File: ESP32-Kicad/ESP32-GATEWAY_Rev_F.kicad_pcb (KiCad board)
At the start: 2 copper layers, 50.8 x 62.2 mm, 97 parts, among them CON1 NA(NH1x20), Q3 Q12MHz/20pF/30ppm/2P/HC-49SM(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, Q4 BC817-40(SOT23), Q5 BC817-40(SOT23), T1 DTC114YKA, U2 SY8089AAAC(SOT23-5), U3 ESP32-WROOM-32D-4MB, U4 LAN8710A-EZC(QFN32), U5 CH340T(SSOP20W)

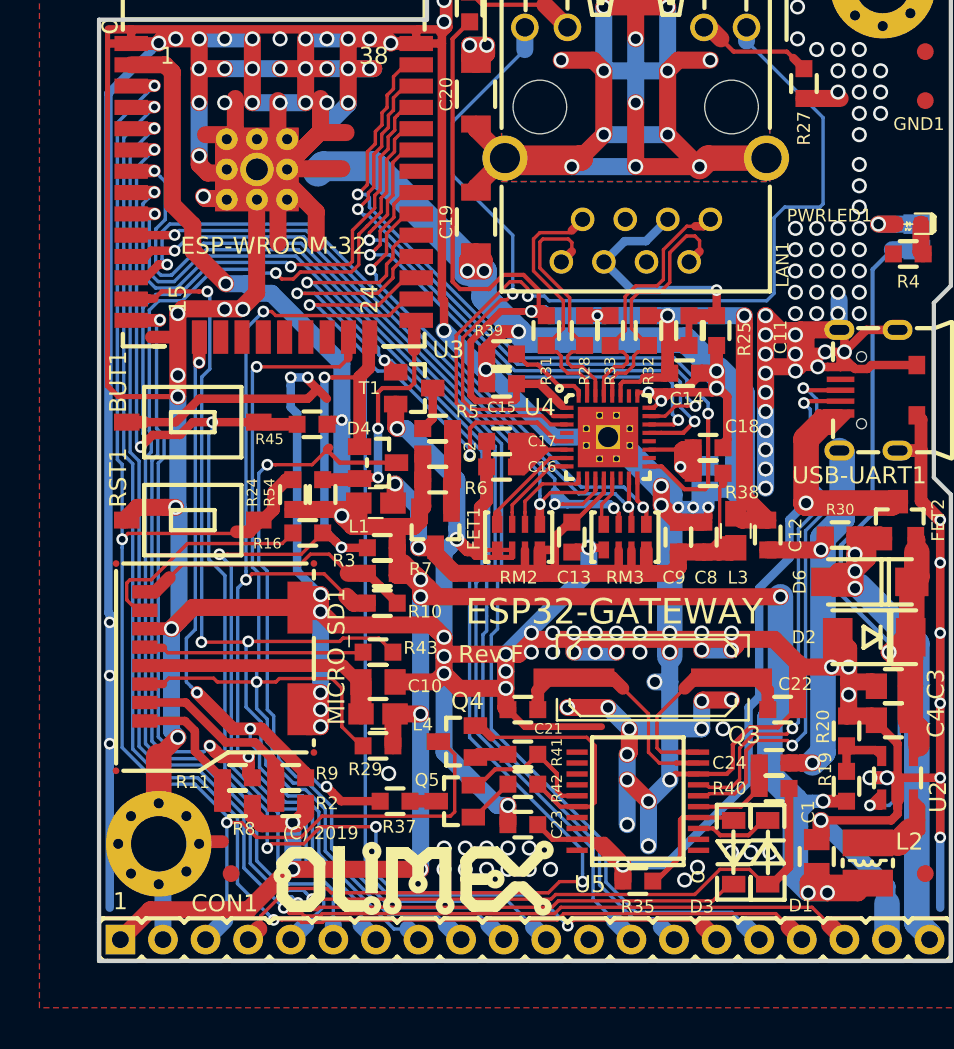
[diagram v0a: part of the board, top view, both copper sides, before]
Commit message: Proyecto de kicad actualizado.
 Se eliminó completamente la sección de la MicroSD
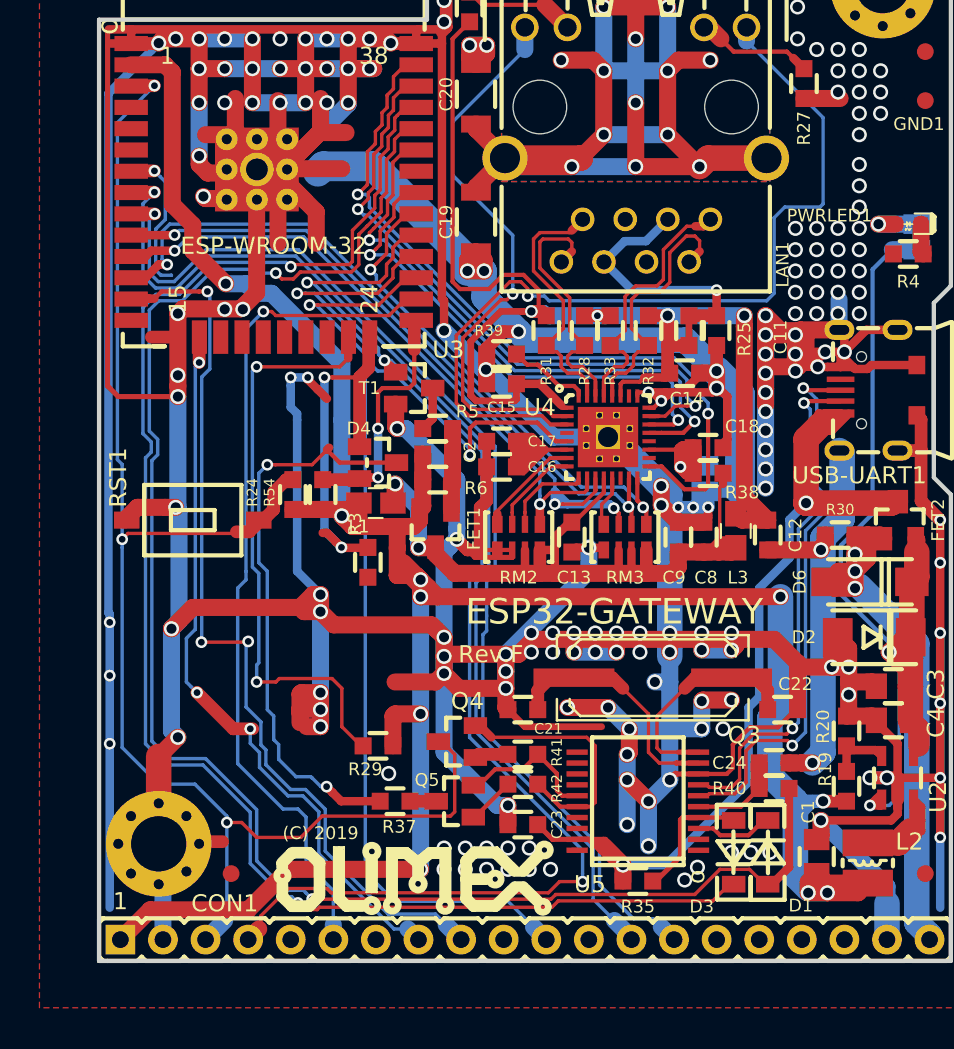
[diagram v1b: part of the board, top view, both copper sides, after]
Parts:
- removed BUT1: T1107A(6x3,8x2,5MM), OLIMEX_Buttons-FP:T1107A(6x3,8x2,5MM)
- removed C10: 47uF/6.3V/20%/X5R/C0805, OLIMEX_RLC-FP:C_0805_5MIL_DWS
- removed L4: FB0805/600R/2A, OLIMEX_RLC-FP:L_0805_5MIL_DWS
- removed MICRO_SD1: TFC-WXCP11-08-LF, OLIMEX_Connectors-FP:TFC-WXCP11-08-LF
- removed R10, R11, R9: NA/R0603, OLIMEX_RLC-FP:R_0603_5MIL_DWS
- removed R16: 220R/R0603, OLIMEX_RLC-FP:R_0603_5MIL_DWS
- removed R2, R7, R8: 2.2k/R0603, OLIMEX_RLC-FP:R_0603_5MIL_DWS
- removed R43: 10R/R0603, OLIMEX_RLC-FP:R_0603_5MIL_DWS
- removed R45: 10k/R0603, OLIMEX_RLC-FP:R_0603_5MIL_DWS
- moved R3 1.22 mm to (85.6, 105.5), turned to 90 degrees
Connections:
- CON1 pad 10: /GPIO15\HS2_CMD -> Net-(CON1-Pad10)
- CON1 pad 15: /GPI34\BUT1 -> Net-(CON1-Pad15)
- CON1 pad 16: /GPI35 -> Net-(CON1-Pad16)
- CON1 pad 17: /GPI36 -> Net-(CON1-Pad17)
- CON1 pad 18: /GPI39 -> Net-(CON1-Pad18)
- CON1 pad 5: /GPIO2\HS2_DATA0 -> Net-(CON1-Pad5)
- CON1 pad 7: /GPIO12\HS2_DATA2 -> Net-(CON1-Pad7)
- R3 pad 1: +3V3 -> GND
- U3 pad 6: /GPI34\BUT1 -> /GPI34
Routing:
- net /GPI34\BUT1: track 88.6 -> 0.00 mm, vias 6 -> 0
- net /GPI39: track 88.3 -> 0.12 mm, vias 2 -> 0
- net /GPI36: track 88.1 -> 0.12 mm, vias 2 -> 0
- net /GPI35: track 74.2 -> 9.01 mm
- net /GPIO12\HS2_DATA2: track 49.1 -> 0.00 mm, vias 3 -> 0
- net /GPIO2\HS2_DATA0: track 56.0 -> 21.9 mm, vias 3 -> 2
- net /GPIO15\HS2_CMD: track 66.7 -> 34.9 mm
- net Net-(MICRO_SD1-Pad8): track 17.2 -> 0.00 mm
- net Net-(C10-Pad1): track 15.3 -> 0.00 mm
- net GND: track 790.1 -> 776.2 mm
- net Net-(MICRO_SD1-Pad7): track 13.5 -> 0.00 mm
- net Net-(MICRO_SD1-Pad5): track 13.2 -> 0.00 mm
- net Net-(MICRO_SD1-Pad2): track 12.6 -> 0.00 mm
- net /GPIO14\HS2_CLK: track 63.6 -> 54.6 mm
- net +3V3: track 168.5 -> 159.8 mm, vias 13 -> 10
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
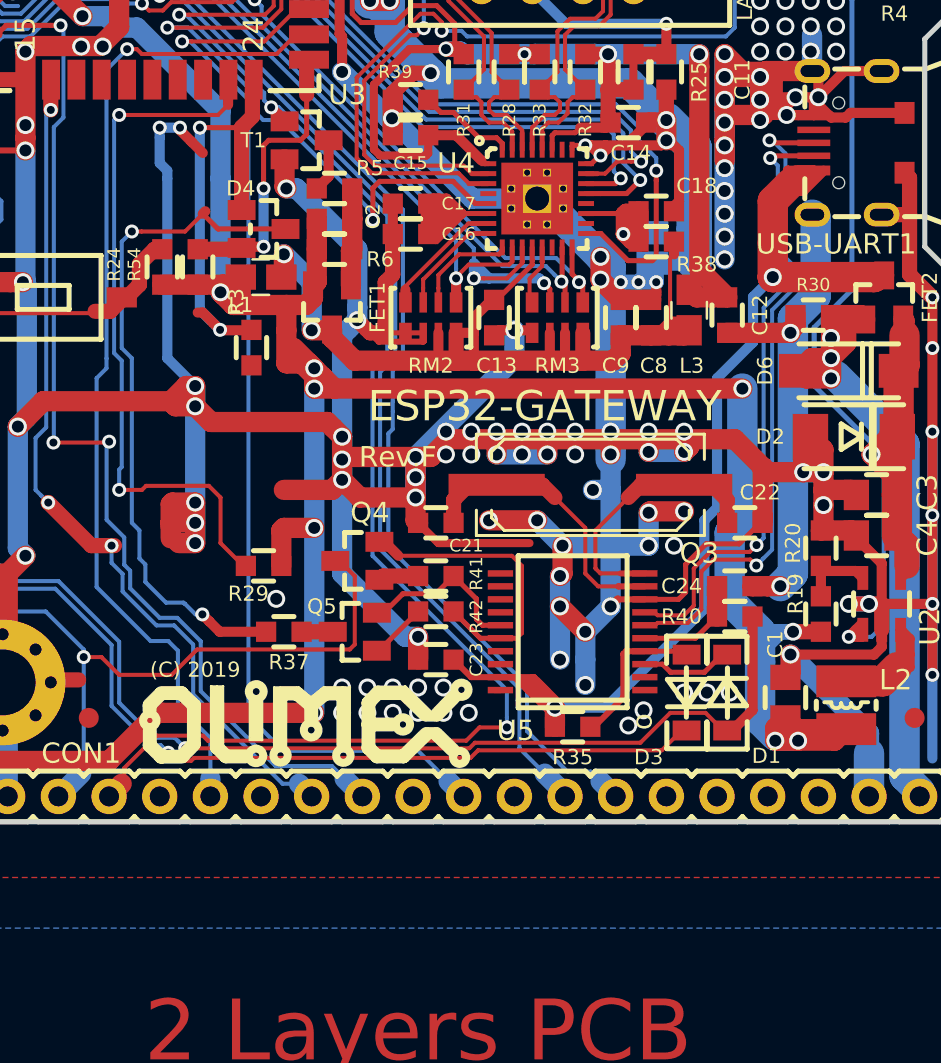
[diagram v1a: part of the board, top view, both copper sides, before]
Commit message: Proyecto de kicad actualizado
Se retiró la parte del programador USB y otras menores asociadas a esta.
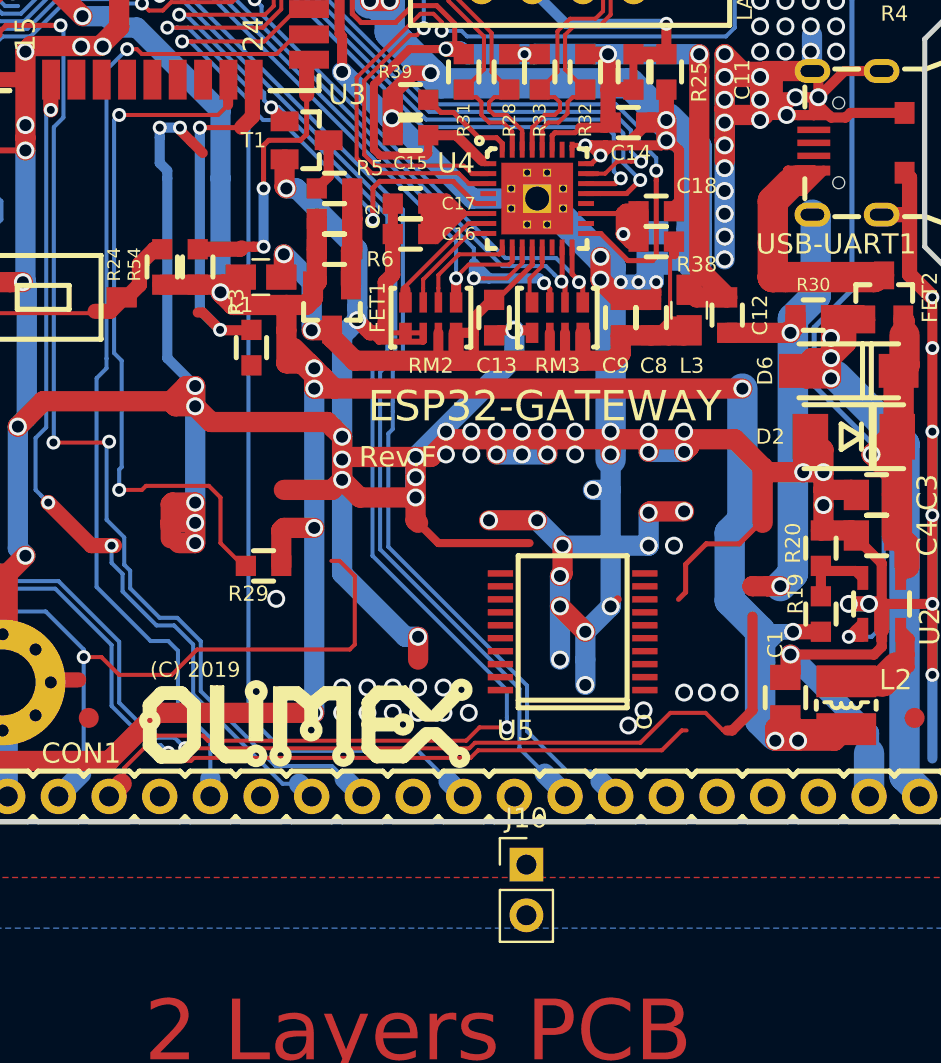
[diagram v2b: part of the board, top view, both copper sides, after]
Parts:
- removed C21, C22: 27pF/50V/5%/C0G/C0603, OLIMEX_RLC-FP:C_0603_5MIL_DWS
- removed C23: 22uF/6.3V/20%/X5R/C0603, OLIMEX_RLC-FP:C_0603_5MIL_DWS
- removed C24: 100nF/50V/20%/Y5V/C0603, OLIMEX_RLC-FP:C_0603_5MIL_DWS
- removed D1, D3: 1N5819S4/SOD123, OLIMEX_Diodes-FP:SOD-123_1C-2A_KA
- removed D4: BAT54C(SOT23-3), OLIMEX_Diodes-FP:SOT23-3
- removed Q3: Q12MHz/20pF/30ppm/2P/HC-49SM(SMD), OLIMEX_Crystal-FP:Q_49U3HMS
- removed Q4, Q5: BC817-40(SOT23), OLIMEX_Transistors-FP:SOT23
- removed R35, R40: 10k/R0603, OLIMEX_RLC-FP:R_0603_5MIL_DWS
- removed R37: 220R/R0603, OLIMEX_RLC-FP:R_0603_5MIL_DWS
- removed R41, R42: 1k/R0603, OLIMEX_RLC-FP:R_0603_5MIL_DWS
- added J10: Conn_01x02_Male, Connector_PinHeader_2.54mm:PinHeader_1x02_P2.54mm_Vertical, F.Cu at (99.4, 131.4)
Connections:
- U5 pad 8: GND -> Net-(U5-Pad8)
- USB-UART1 pad 2: Net-(U5-Pad7) -> Net-(USB-UART1-Pad2)
- USB-UART1 pad 3: Net-(U5-Pad6) -> Net-(USB-UART1-Pad3)
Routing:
- net /+5V_USB: track 58.6 -> 19.1 mm, vias 2 -> 0
- net /D_Com: track 33.9 -> 0.00 mm, vias 2 -> 0
- net Net-(U5-Pad6): track 33.4 -> 0.00 mm, vias 2 -> 0
- net Net-(U5-Pad7): track 30.8 -> 0.00 mm, vias 2 -> 0
- net Net-(U5-Pad16): track 15.1 -> 0.00 mm
- net Net-(U5-Pad9): track 14.4 -> 0.00 mm
- net Net-(U5-Pad10): track 14.3 -> 0.00 mm
- net Net-(U5-Pad15): track 8.58 -> 0.00 mm
- net Net-(U5-Pad4): track 7.75 -> 0.00 mm
- net Net-(U5-Pad5): track 5.59 -> 0.00 mm
- net Net-(U5-Pad3): track 4.66 -> 0.00 mm
- net /GPIO2\HS2_DATA0: track 21.9 -> 17.8 mm
- net GND: track 776.2 -> 773.2 mm
- net Net-(Q5-Pad1): track 2.88 -> 0.00 mm
- net Net-(Q4-Pad1): track 2.02 -> 0.00 mm
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
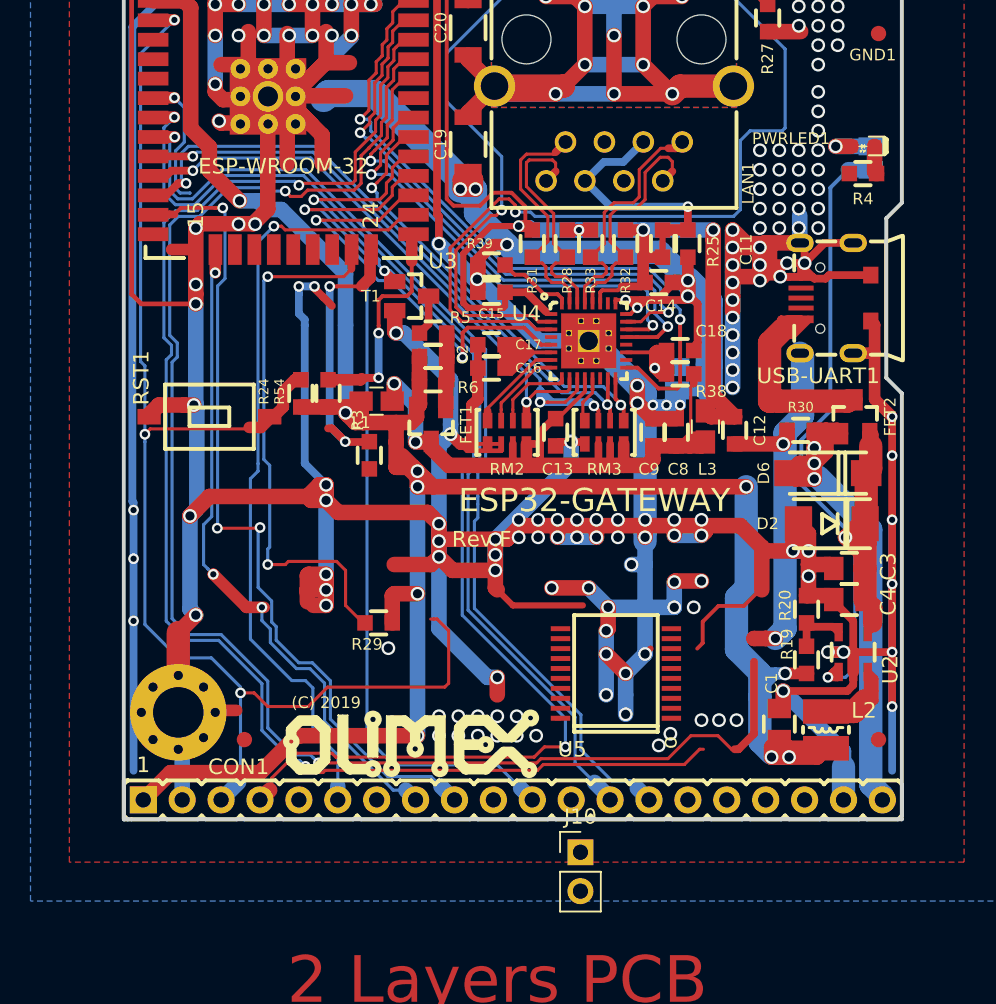
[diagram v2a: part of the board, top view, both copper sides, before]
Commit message: Proyecto de Kicad actualizado
Fuente corregida. Programador agregado. Cambios menores.
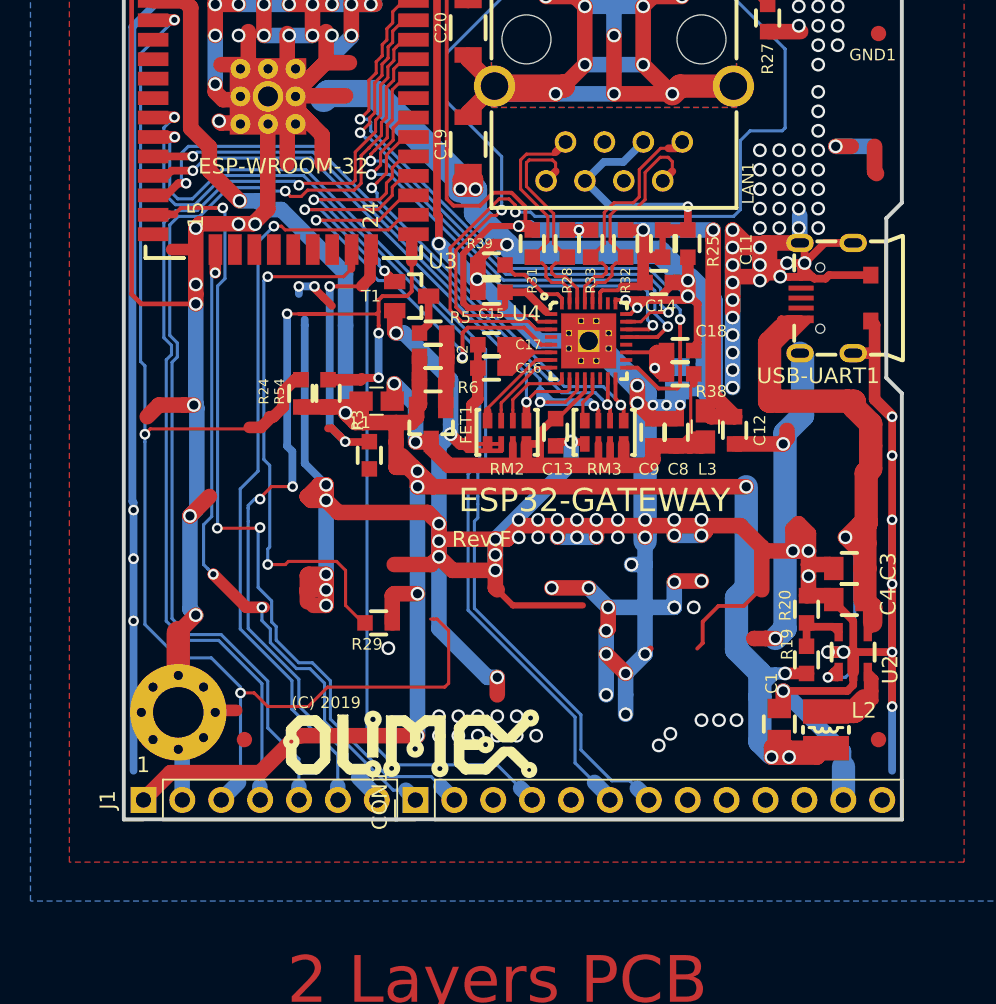
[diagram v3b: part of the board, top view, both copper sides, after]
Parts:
- removed D2: SMBJ6.0A(DO-214AA), OLIMEX_Diodes-FP:DO214AA_1(K)-2(A)
- removed D6: 1N5822/SS34/SMA, OLIMEX_Diodes-FP:SMA-KA
- removed FET2: WPM2015-3/TR, OLIMEX_Transistors-FP:SOT23
- removed J10: Conn_01x02_Male, Connector_PinHeader_2.54mm:PinHeader_1x02_P2.54mm_Vertical
- removed LED_E1: Closed, OLIMEX_Jumpers-FP:SJ
- removed PWRLED1: LED/RED/0603, OLIMEX_LEDs-FP:LED_0603_KA
- removed R30: 1M/R0603, OLIMEX_RLC-FP:R_0603_5MIL_DWS
- removed R4: 2.2k/R0603, OLIMEX_RLC-FP:R_0603_5MIL_DWS
- removed RST1: T1107A(6x3,8x2,5MM), OLIMEX_Buttons-FP:T1107A(6x3,8x2,5MM)
- removed U5: CH340T(SSOP20W), OLIMEX_IC-FP:SSOP-20W
- added J1: Conn_01x07_Male, Connector_PinHeader_2.54mm:PinHeader_1x07_P2.54mm_Vertical, F.Cu at (70.9, 128.0)
- C1: value 47uF/6.3V/20%/X5R/C0805 -> 10uF/6.3V/20%/X5R/C0805/1mΩ
- C3, C4: value 47uF/6.3V/20%/X5R/C0805 -> 4.7uF/6.3V/20%/X5R/C0805/1mΩ
- CON1: value NA(NH1x20) -> Conn_01x13_Male; footprint OLIMEX_Connectors-FP:HN1x20 -> Connector_PinHeader_2.54mm:PinHeader_1x13_P2.54mm_Vertical
- L2: value 2.2uH/1.5A/DCR=72mR/20%/3.00x3.00x1.50mm/CD32(NR3015T2R2M) -> 2.2uH/1.5A/DCR=35mR/20%/3.00x3.00x1.50mm/CD32(NR3015T2R2M)
- R19: value 220k/R0603 -> 442k/1%/50mW/R0603
- R20: value 49.9k/1%/R0603 -> 100k/1%/63mw/R0603
- R54: value NA/R0603 -> 10K/R0603
- U2: value SY8089AAAC(SOT23-5) -> TLV62569DBVT(SOT23-5)
- moved CON1 6.36 mm to (88.6, 128.0), turned to 90 degrees
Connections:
- CON1 pad 1: +3V3 -> /GPIO13\HS2_DATA3
- CON1 pad 11: /GPIO16 -> Net-(CON1-Pad11)
- CON1 pad 12: Net-(CON1-Pad12) -> GND
- CON1 pad 13: /GPIO32 -> Net-(CON1-Pad13)
- CON1 pad 2: GND -> /GPIO14\HS2_CLK
- CON1 pad 3: /ESP_EN -> Net-(CON1-Pad3)
- CON1 pad 4: /GPIO5\PHY_PWR -> /GPIO16
- CON1 pad 6: /GPIO4\HS2_DATA1 -> /GPIO32
- CON1 pad 7: Net-(CON1-Pad7) -> /GPIO33\LED
- CON1 pad 8: /GPIO13\HS2_DATA3 -> Net-(CON1-Pad8)
- CON1 pad 9: /GPIO14\HS2_CLK -> Net-(CON1-Pad9)
- USB-UART1 pad 1: /+5V_USB -> +5V
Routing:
- net /GPIO5\PHY_PWR: track 75.0 -> 16.2 mm, vias 3 -> 2
- net /GPIO0: track 14.6 -> 59.4 mm, vias 2 -> 5
- net +5V_EXT: track 39.9 -> 0.00 mm, vias 3 -> 0
- net /GPIO3\U0RXD: track 100.0 -> 66.8 mm, vias 2 -> 1
- net /GPIO1\U0TXD: track 93.2 -> 69.1 mm, vias 2 -> 1
- net /+5V_USB: track 19.1 -> 0.00 mm
- net +5V: track 64.9 -> 55.0 mm, vias 3 -> 2
- net /GPI35: track 9.01 -> 0.00 mm, vias 1 -> 0
- net Net-(PWRLED1-Pad1): track 1.83 -> 0.00 mm
- net GND: track 773.2 -> 771.6 mm, vias 197 -> 198

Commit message: Proyecto de kicad actualizado.
Se agregaron los conectores adecuados y se rutearon los gpio para estos. Queda pendiente ubicarlos correctamente para evitar el solapamiento de estos. Se acomodaron algunas resistencias y se eliminaron pistas viejas innecesarias.
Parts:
- removed CON1: Conn_01x13_Male, Connector_PinHeader_2.54mm:PinHeader_1x13_P2.54mm_Vertical
- removed USB-UART1: MISB-SWMM-5B-LF(USB_MICRO), OLIMEX_Connectors-FP:USB-MICRO_MISB-SWMM-5B_LF
- added PUERTA1: Conn_01x02_Female, Connector_Molex:Molex_KK-254_AE-6410-02A_1x02_P2.54mm_Vertical, F.Cu at (107.3, 124.6)
- added PUERTA2: Conn_01x02_Female, Connector_Molex:Molex_KK-254_AE-6410-02A_1x02_P2.54mm_Vertical, F.Cu at (103.6, 124.6)
- added TEMP1: Conn_01x03_Female, Connector_Molex:Molex_KK-254_AE-6410-03A_1x03_P2.54mm_Vertical, F.Cu at (95.4, 122.3)
- added TEMP2: Conn_01x03_Female, Connector_Molex:Molex_KK-254_AE-6410-03A_1x03_P2.54mm_Vertical, F.Cu at (91.6, 122.2)
- added USB-UART2: USB_B_Micro, Connector_USB:USB_Micro-B_Amphenol_10104110_Horizontal, F.Cu at (115.5, 95.3)
- J1: footprint Connector_PinHeader_2.54mm:PinHeader_1x07_P2.54mm_Vertical -> Connector_PinHeader_2.54mm:PinHeader_1x07_P2.54mm_Horizontal
- moved R29 19.8 mm to (79.0, 98.0)
- moved Logo-OlimexBIG 13.6 mm to (79.1, 114.5)
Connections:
- U3 pad 13: /GPIO14\HS2_CLK -> /GPIO14\TEMP2
- U3 pad 16: /GPIO13\HS2_DATA3 -> /GPIO13\TEMP1
- U3 pad 8: /GPIO32 -> /GPIO32\PUERTA1
- U3 pad 9: /GPIO33\LED -> /GPIO33\PUERTA2
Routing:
- net /GPIO32\PUERTA1: track 0.00 -> 77.9 mm, vias 0 -> 1
- net /GPIO33\PUERTA2: track 0.00 -> 69.3 mm, vias 0 -> 1
- net /GPIO32: track 66.7 -> 0.00 mm, vias 1 -> 0
- net /GPIO33\LED: track 66.7 -> 0.00 mm, vias 1 -> 0
- net /GPIO14\TEMP2: track 0.00 -> 55.4 mm, vias 0 -> 3
- net /GPIO14\HS2_CLK: track 54.6 -> 0.00 mm, vias 3 -> 0
- net /GPIO13\TEMP1: track 0.00 -> 52.9 mm, vias 0 -> 3
- net /GPIO13\HS2_DATA3: track 43.7 -> 0.00 mm, vias 3 -> 0
- net /GPIO15\HS2_CMD: track 34.9 -> 12.9 mm, vias 2 -> 0
- net /ESP_EN: track 89.9 -> 70.4 mm, vias 3 -> 2
- net /GPIO16: track 54.9 -> 44.9 mm
- net +3V3: track 159.8 -> 168.9 mm, vias 10 -> 11
- net GND: vias 198 -> 190
